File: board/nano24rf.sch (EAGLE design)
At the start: 20 parts

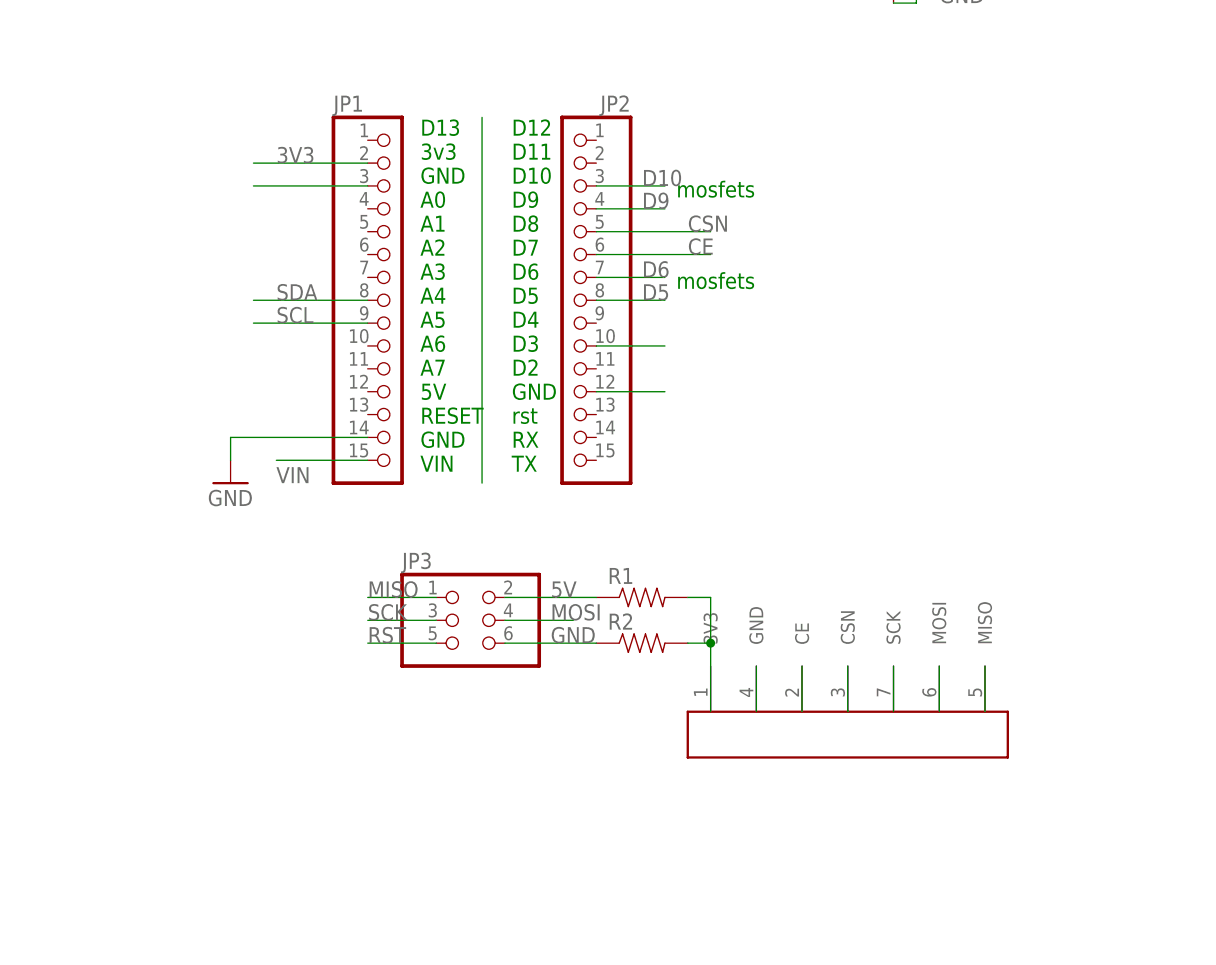
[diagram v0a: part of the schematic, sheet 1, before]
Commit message: fixed bad packges for 2x3 and smdx07
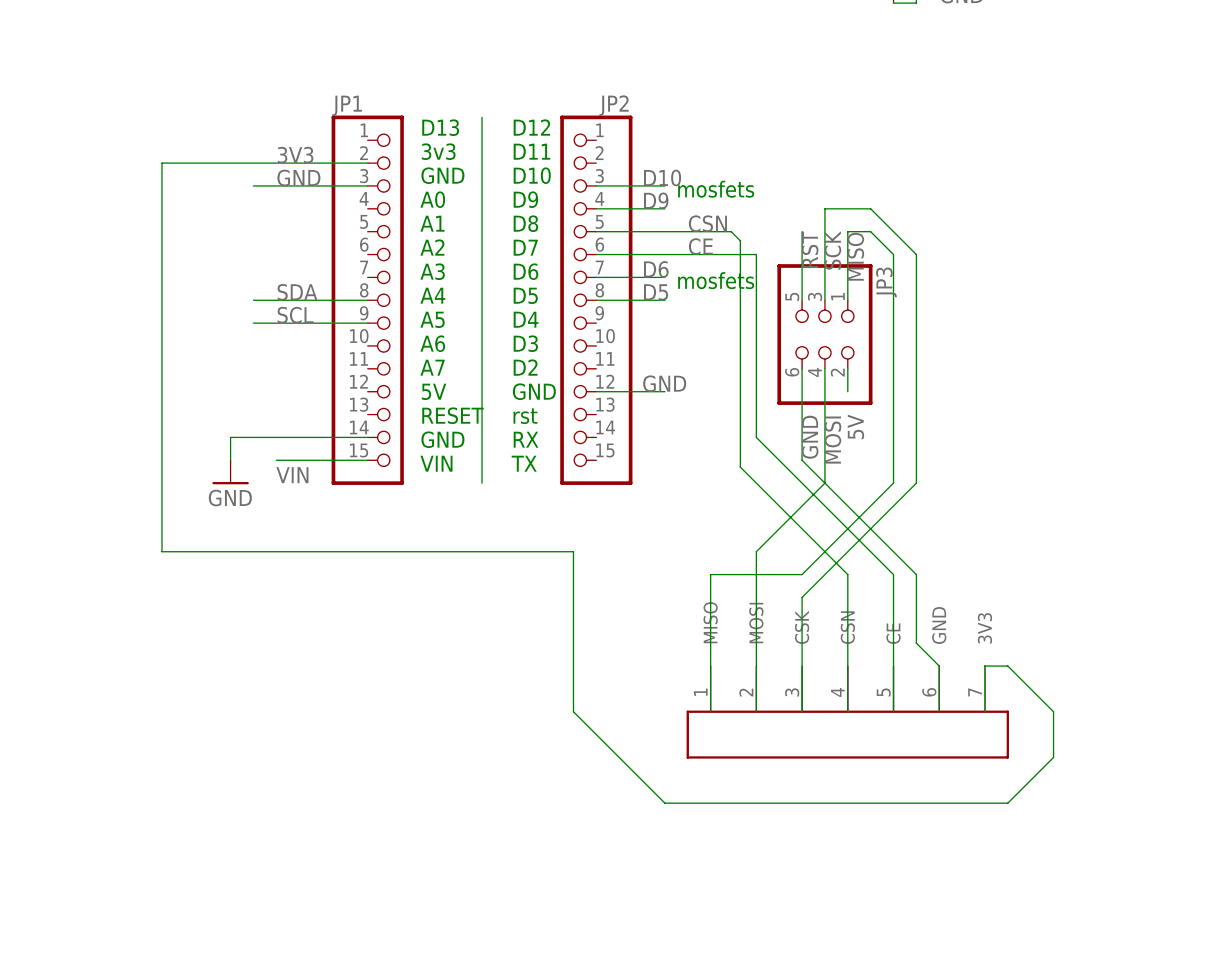
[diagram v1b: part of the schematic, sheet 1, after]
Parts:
- removed R1, R2: (no value), ATTAMI-V0.00:RESISTOR0805-RES
- renumbered U$6 to MOSFET-34, U$7 to RF24, U$8 to MOSFET-12
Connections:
- removed net D3: JP2.10
- removed net N$6: R1.2, R2.2, RF24.3V3
- net 3V3: now also RF24.3V3
- net 5V: no longer R1.1
- net GND: no longer R2.1
- net SCK: now also RF24.CSK; no longer RF24.SCK
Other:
- moved on the sheet: JP3

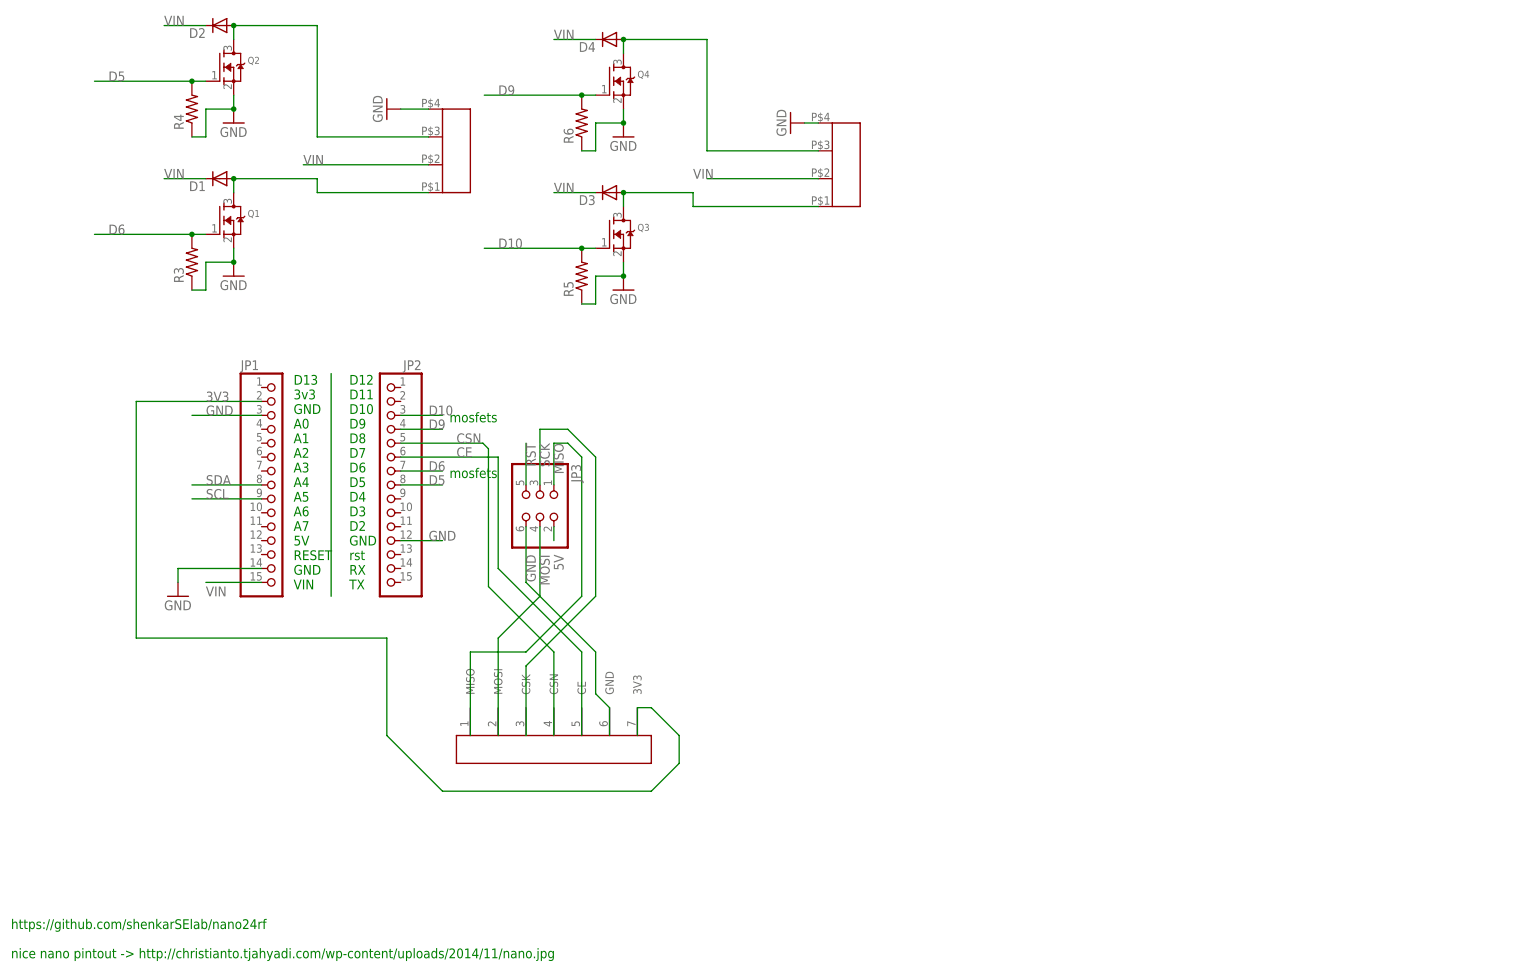
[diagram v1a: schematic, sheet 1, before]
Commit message: routed ver3, no canstlation
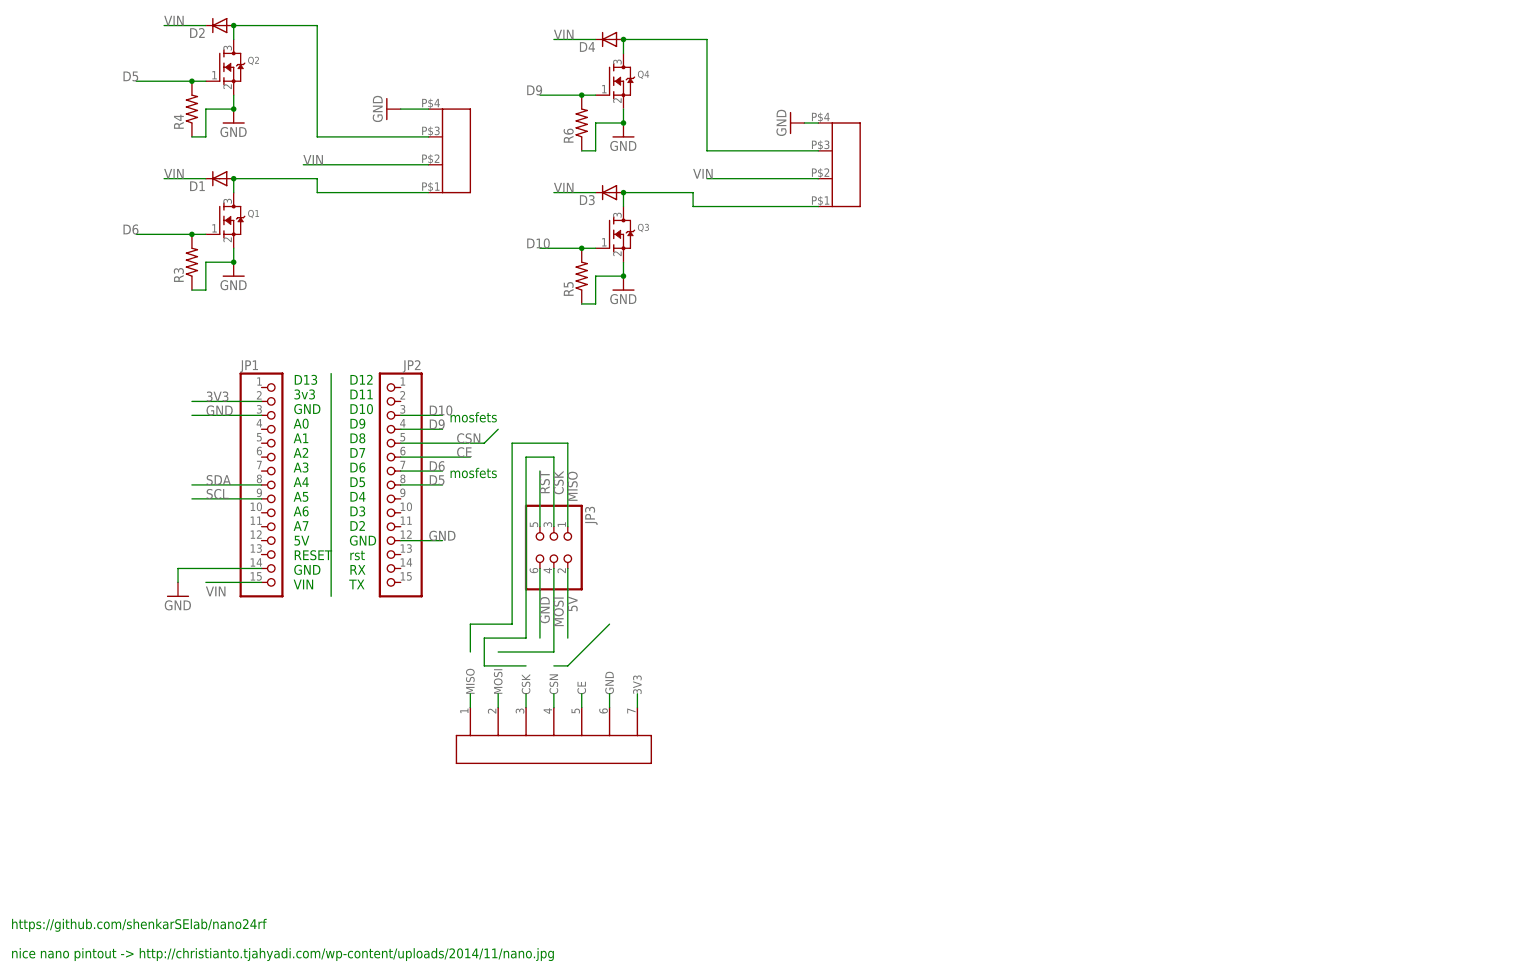
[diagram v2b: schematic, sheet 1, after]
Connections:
- net SCK renamed CSK
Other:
- moved on the sheet: JP3

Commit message: added gerber for cestlation fike
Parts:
- JP1, JP2: device microbuilder:HEADER-1X15 -> nano24rf:HEADER-1X15LONG
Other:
- moved on the sheet: JP1, JP2
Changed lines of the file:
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@@
 <part name="U$3" library="ATTAMI-V0.00" deviceset="GND" device=""/>
 <part name="U$5" library="ATTAMI-V0.00" deviceset="GND" device=""/>
-<part name="JP1" library="microbuilder" deviceset="HEADER-1X15" device=""/>
-<part name="JP2" library="microbuilder" deviceset="HEADER-1X15" device=""/>
+<part name="JP1" library="nano24rf" deviceset="HEADER-1X15" device="LONG"/>
+<part name="JP2" library="nano24rf" deviceset="HEADER-1X15" device="LONG"/>
 <part name="JP3" library="nano24rf" deviceset="PINHD-2X3" device="SMT"/>
 <part name="RF24" library="nano24rf" deviceset="1X7-SMDPADS" device=""/>

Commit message: back to round ads
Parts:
- JP1, JP2: device nano24rf:HEADER-1X15LONG -> nano24rf:HEADER-1X15RND
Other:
- moved on the sheet: JP1, JP2
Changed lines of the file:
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@@
 <part name="U$3" library="ATTAMI-V0.00" deviceset="GND" device=""/>
 <part name="U$5" library="ATTAMI-V0.00" deviceset="GND" device=""/>
-<part name="JP1" library="nano24rf" deviceset="HEADER-1X15" device="LONG"/>
-<part name="JP2" library="nano24rf" deviceset="HEADER-1X15" device="LONG"/>
+<part name="JP1" library="nano24rf" deviceset="HEADER-1X15" device="RND"/>
+<part name="JP2" library="nano24rf" deviceset="HEADER-1X15" device="RND"/>
 <part name="JP3" library="nano24rf" deviceset="PINHD-2X3" device="SMT"/>
 <part name="RF24" library="nano24rf" deviceset="1X7-SMDPADS" device=""/>

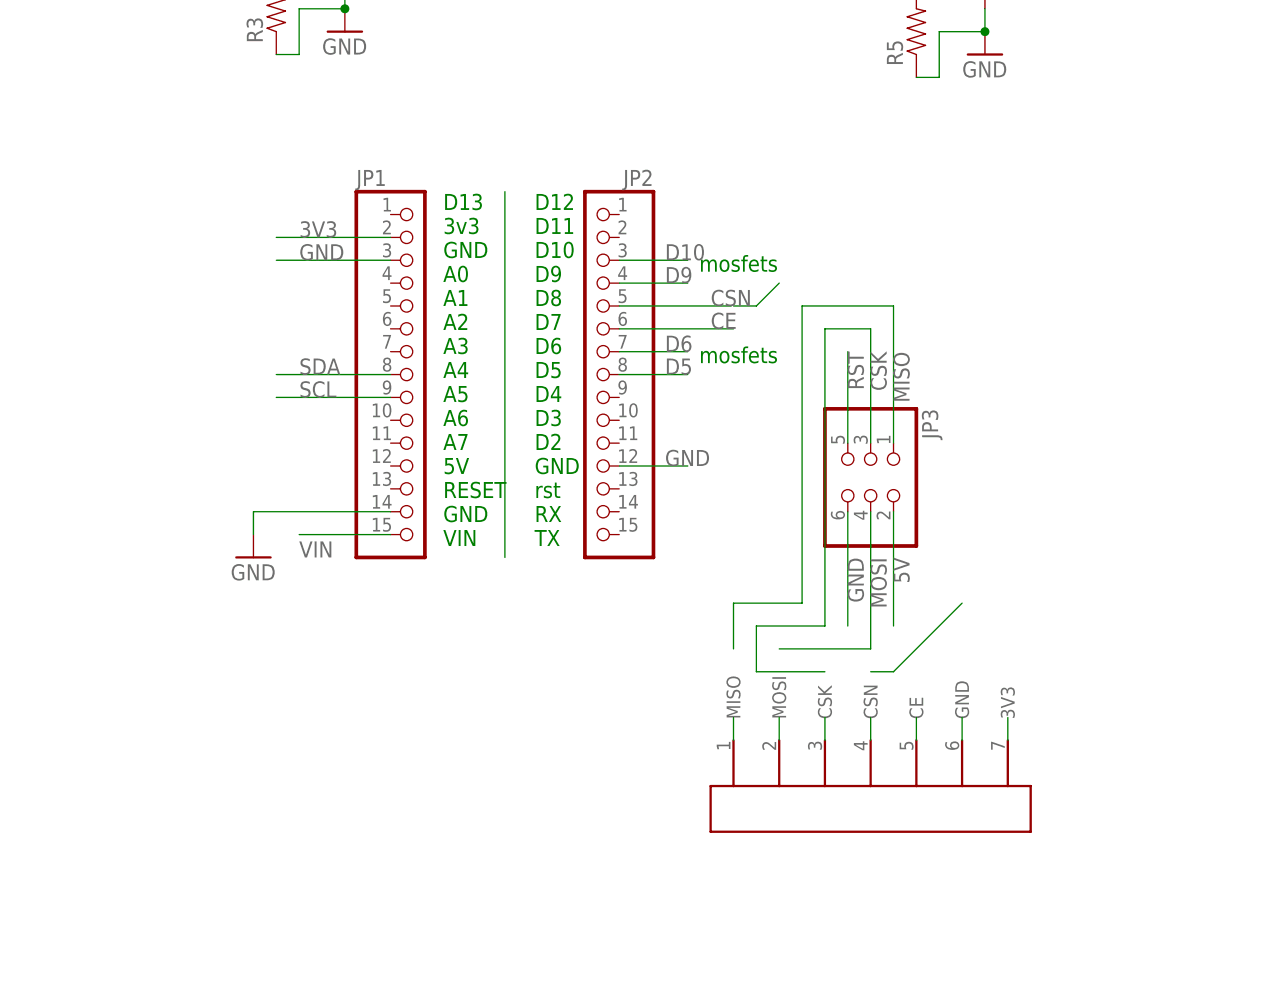
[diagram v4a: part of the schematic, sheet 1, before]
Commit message: long pads
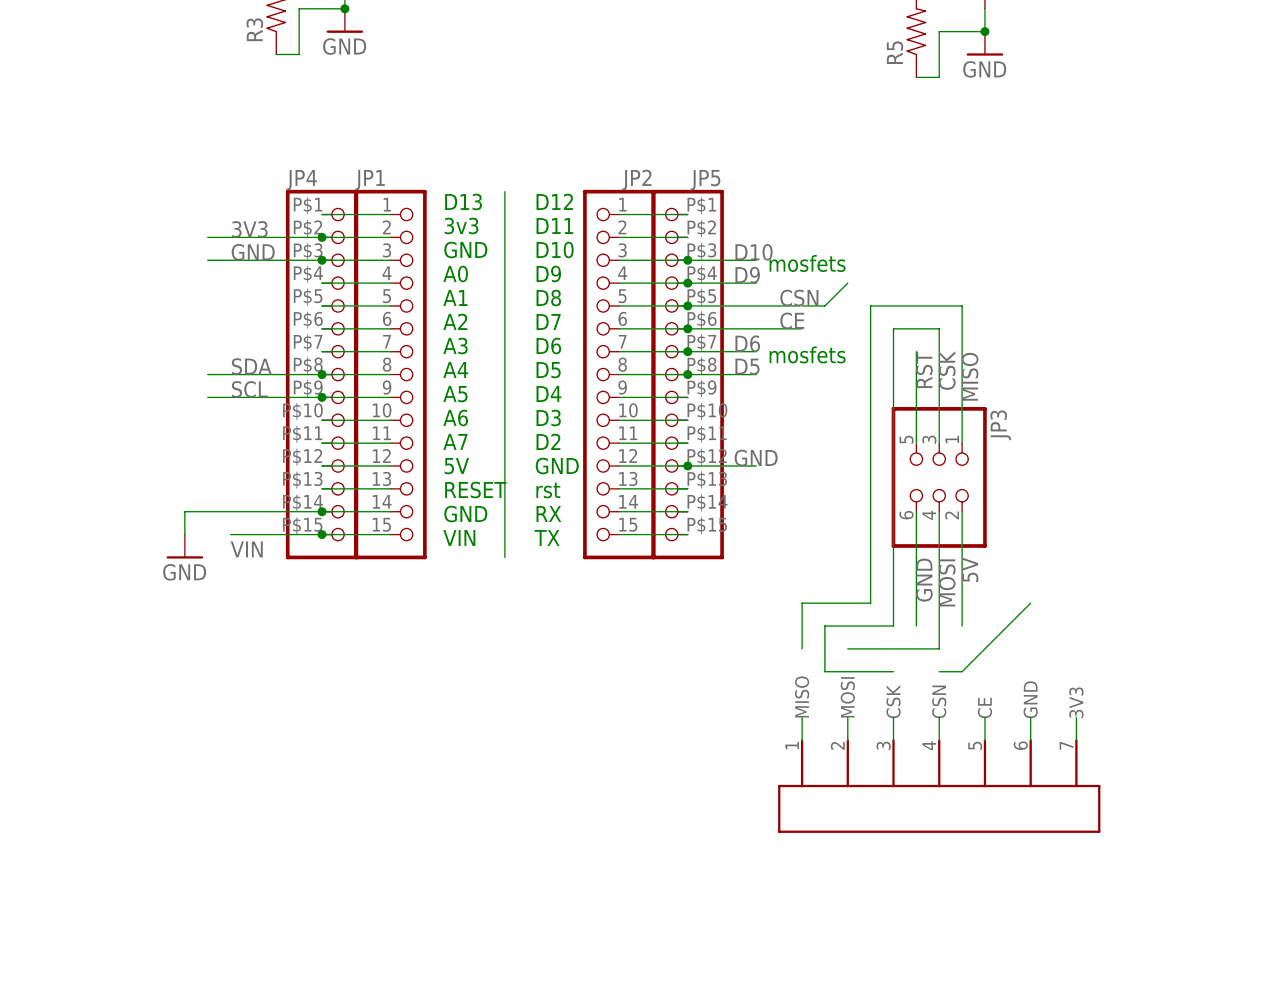
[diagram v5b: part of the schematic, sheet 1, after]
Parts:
- added JP4, JP5: (no value), nano24rf:HEADER-1X15LONG
- MOSFET-12, MOSFET-34: value FATPAD4 -> FATPAD4LONG; device nano24rf:FATPAD4 -> nano24rf:FATPAD4LONG
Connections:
- new net N$10: JP1.11, JP4.11
- new net N$11: JP1.12, JP4.12
- new net N$12: JP1.13, JP4.13
- new net N$13: JP2.15, JP5.15
- new net N$14: JP2.14, JP5.14
- new net N$15: JP2.13, JP5.13
- new net N$16: JP2.11, JP5.11
- new net N$17: JP2.10, JP5.10
- new net N$18: JP2.9, JP5.9
- new net N$19: JP2.2, JP5.2
- new net N$20: JP2.1, JP5.1
- new net N$4: JP1.1, JP4.1
- new net N$5: JP1.4, JP4.4
- new net N$6: JP1.5, JP4.5
- new net N$7: JP1.6, JP4.6
- new net N$8: JP1.7, JP4.7
- new net N$9: JP1.10, JP4.10
- net 3V3: now also JP4.2
- net CE: now also JP5.6
- net CSN: now also JP5.5
- net D10: now also JP5.3
- net D5: now also JP5.8
- net D6: now also JP5.7
- net D9: now also JP5.4
- net GND: now also JP4.14, JP4.3, JP5.12
- net SCL: now also JP4.9
- net SDA: now also JP4.8
- net VIN: now also JP4.15
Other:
- moved on the sheet: JP3

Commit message: slight schema re-arange, and gerber
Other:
- note added: "https://github.com/shenkarSElab/nano24rf"
- note removed: "https://github.com/shenkarSElab/nano24rf nice nano pintout -> http://christianto.tjahyadi.com/wp-content/uploads/2014/11/nano.jpg"
- moved on the sheet: D1, D2, D3, D4, JP3, Q1, Q2, Q3, Q4, R3, R4, R5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
